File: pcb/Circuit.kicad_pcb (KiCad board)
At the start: 2 copper layers, 82.4 x 68.9 mm, 47 parts, among them J1 DTM13-12PA-R008, J2 TSW-101-07-T-D, J3 TSW-101-07-T-D, U1 MCP1700-1802E_TO92, U2 CDP68HC68S1, U3 LM2672N-5.0, U4 Teensy4.0, U5 MCP2562-H-P

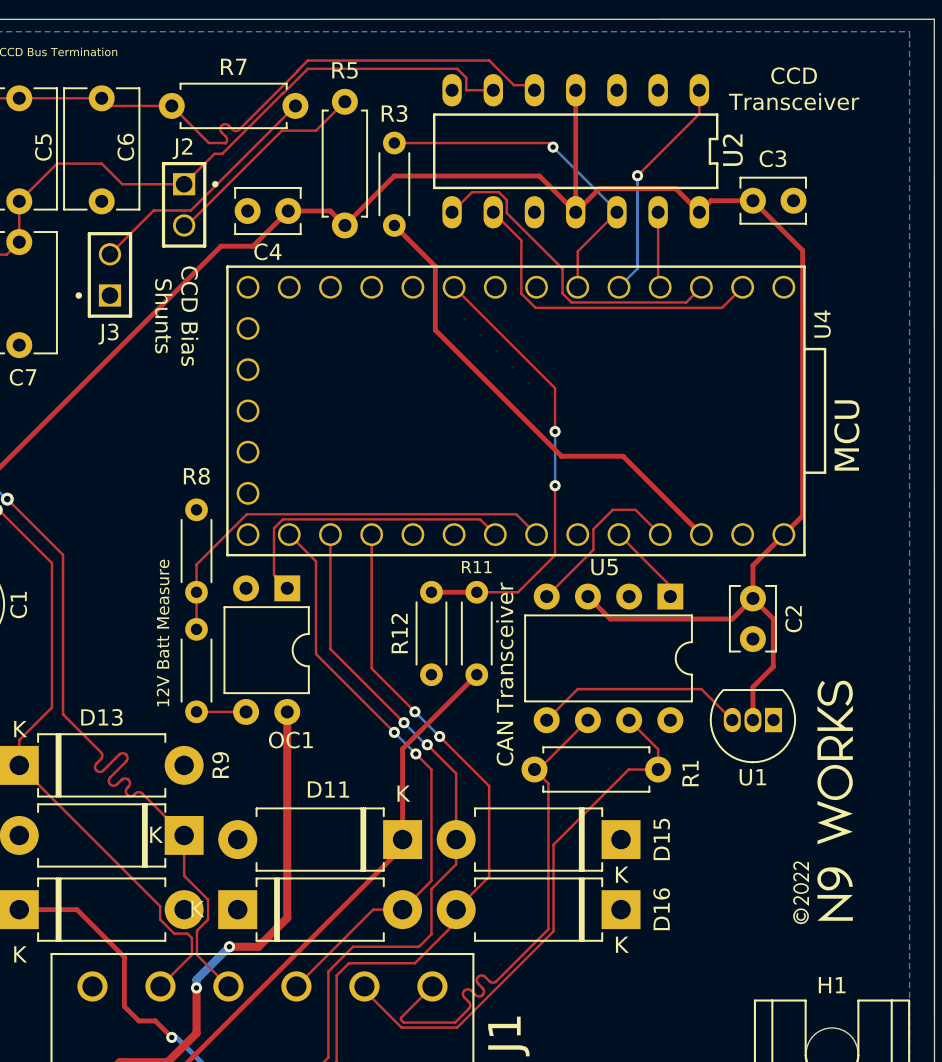
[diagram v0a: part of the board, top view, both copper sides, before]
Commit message: Add overvoltage protection to the 12v measure pin
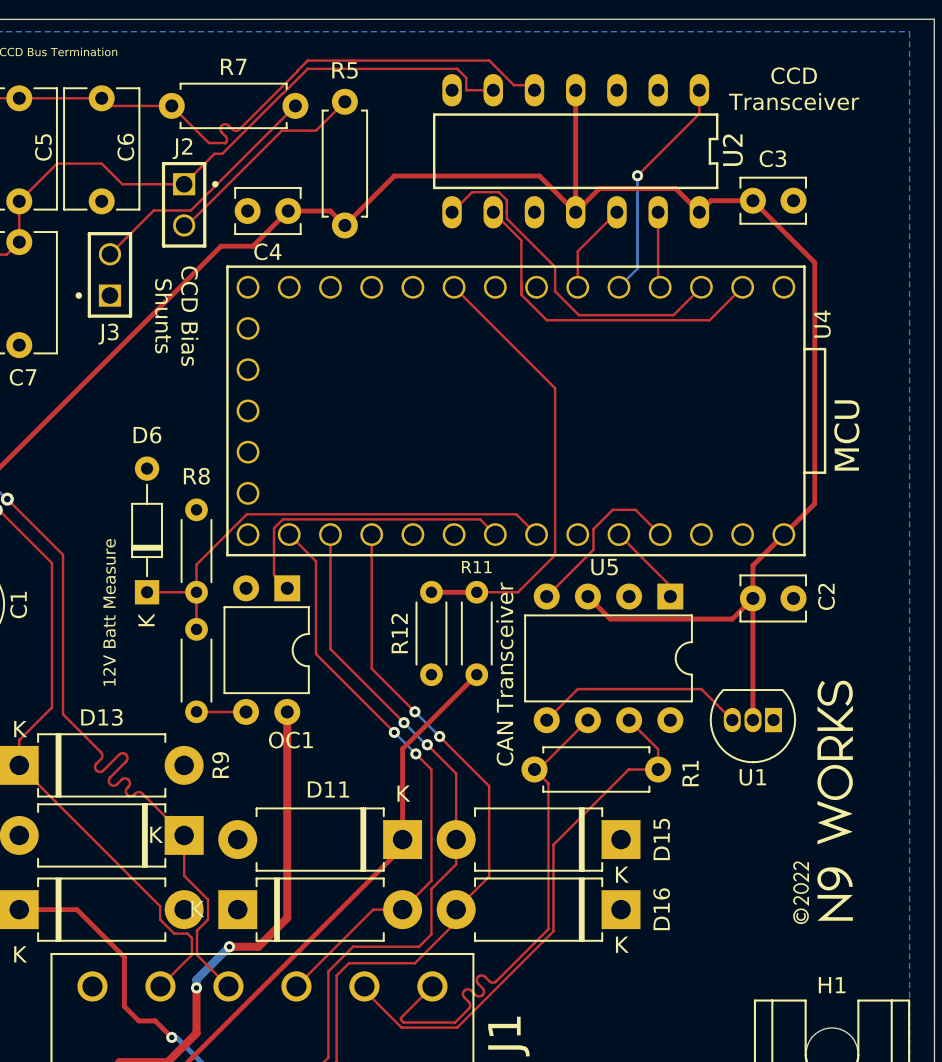
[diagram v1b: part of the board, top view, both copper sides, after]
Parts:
- removed R3: 10k, Resistor_THT:R_Axial_DIN0204_L3.6mm_D1.6mm_P5.08mm_Horizontal
- added D6: 3.3v Shottky, Diode_THT:D_DO-34_SOD68_P7.62mm_Horizontal, F.Cu at (84.1, 101.9)
- turned C2 to 0 degrees
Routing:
- net 3v3: track 29.1 -> 0.00 mm
- net idle: track 21.2 -> 5.62 mm, vias 1 -> 0
- net 12V_MEASURE: track 26.7 -> 29.8 mm
- net rxd: track 20.3 -> 21.6 mm
- net txd: track 20.4 -> 21.5 mm
- net SPEEDO: track 28.0 -> 27.7 mm, vias 2 -> 0

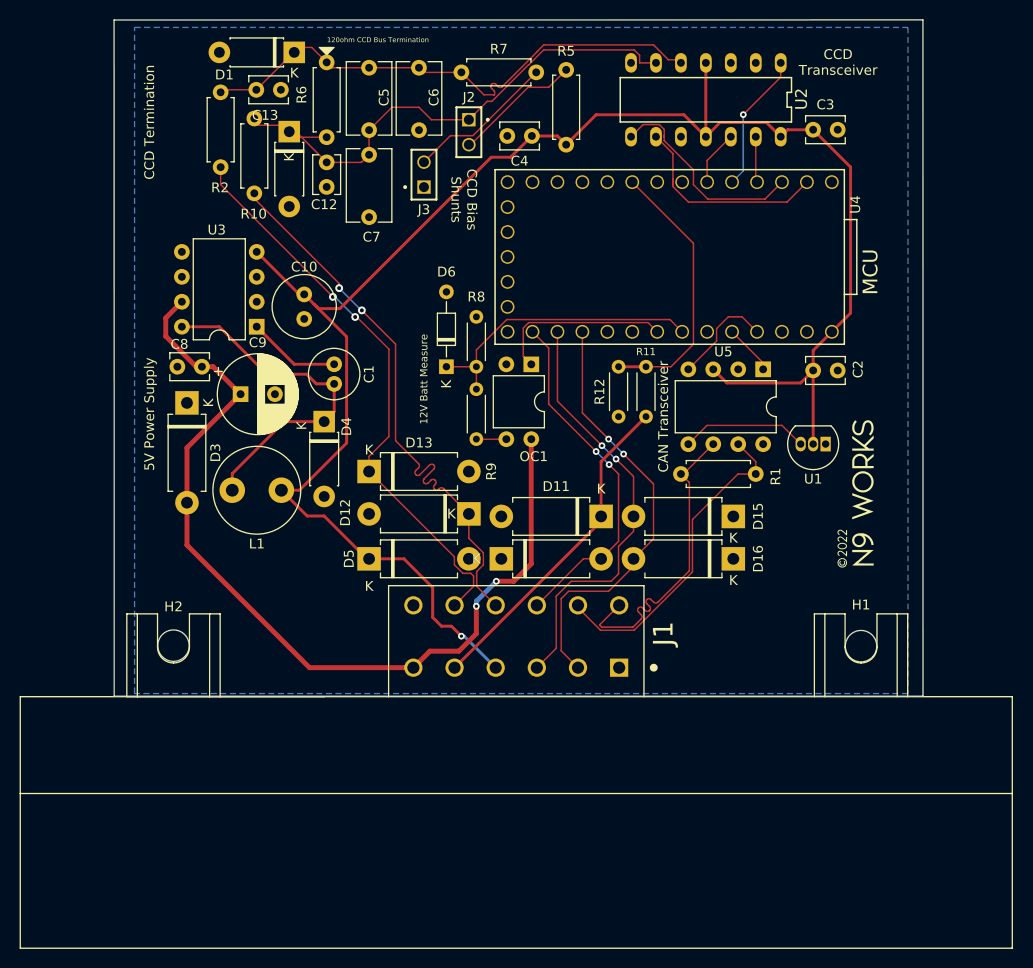
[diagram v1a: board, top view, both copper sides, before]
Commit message: Add 3.3v overvolt protection zeners
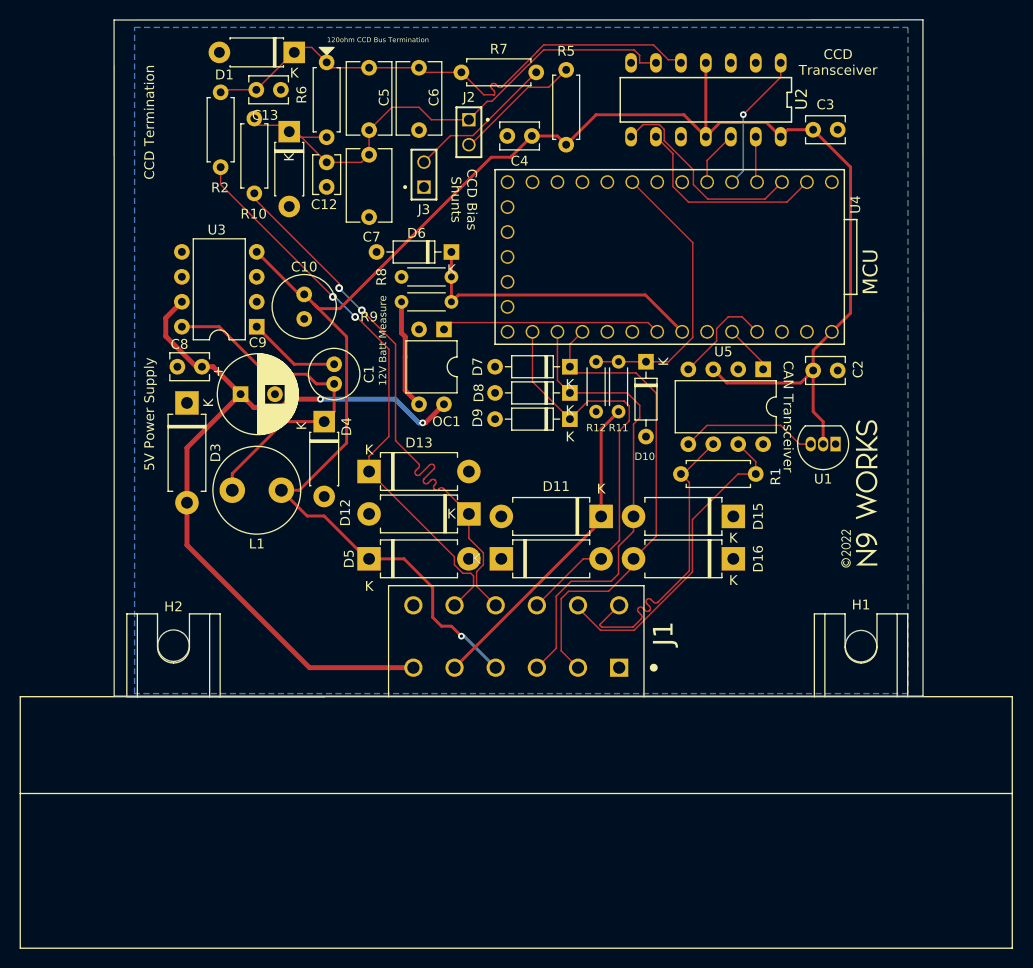
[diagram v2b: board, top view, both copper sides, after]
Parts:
- added D10: 3.3v, Diode_THT:D_DO-35_SOD27_P7.62mm_Horizontal, F.Cu at (104.4, 101.3)
- added D7: 3.3v, Diode_THT:D_DO-35_SOD27_P7.62mm_Horizontal, F.Cu at (96.6, 101.9)
- added D8: 3.3v, Diode_THT:D_DO-35_SOD27_P7.62mm_Horizontal, F.Cu at (96.6, 104.5)
- added D9: 3.3v, Diode_THT:D_DO-35_SOD27_P7.62mm_Horizontal, F.Cu at (96.6, 107.2)
- D6: value 3.3v Shottky -> 3.3v; footprint Diode_THT:D_DO-34_SOD68_P7.62mm_Horizontal -> Diode_THT:D_DO-35_SOD27_P7.62mm_Horizontal
- R8: value 1.5M -> 2.2Kohm
- R9: value 10M -> 13Kohm
- moved D6 11.7 mm to (84.6, 90.2), turned to 180 degrees
- moved OC1 9.57 mm to (83.8, 98.1)
- moved R8 9.49 mm to (84.6, 92.7), turned to 180 degrees
- moved R9 9.25 mm to (84.6, 95.2), turned to 180 degrees
- moved R11 2.84 mm to (101.6, 101.3)
- moved R12 2.34 mm to (99.3, 106.4)
- moved U1 1.02 mm to (123.7, 109.7)
- moved     0.38 mm to (126.1, 114.8)
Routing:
- net Net-(OC1-Pad3): track 3.06 -> 11.2 mm
- net +12V: track 91.1 -> 83.5 mm
- net IO/3: track 36.0 -> 42.7 mm, vias 2 -> 0
- net IO/1: track 44.2 -> 49.0 mm, vias 2 -> 0
- net 12V_MEASCTL: track 18.3 -> 22.4 mm
- net IO/2: track 43.9 -> 47.8 mm, vias 2 -> 0
- net SPEEDO: track 27.7 -> 29.2 mm
- net /1v8: track 13.0 -> 14.0 mm
- net rxd: track 21.6 -> 20.9 mm
- net SPEEDO_IN: track 33.6 -> 33.0 mm
- net 12V_MEASURE: track 29.8 -> 30.4 mm

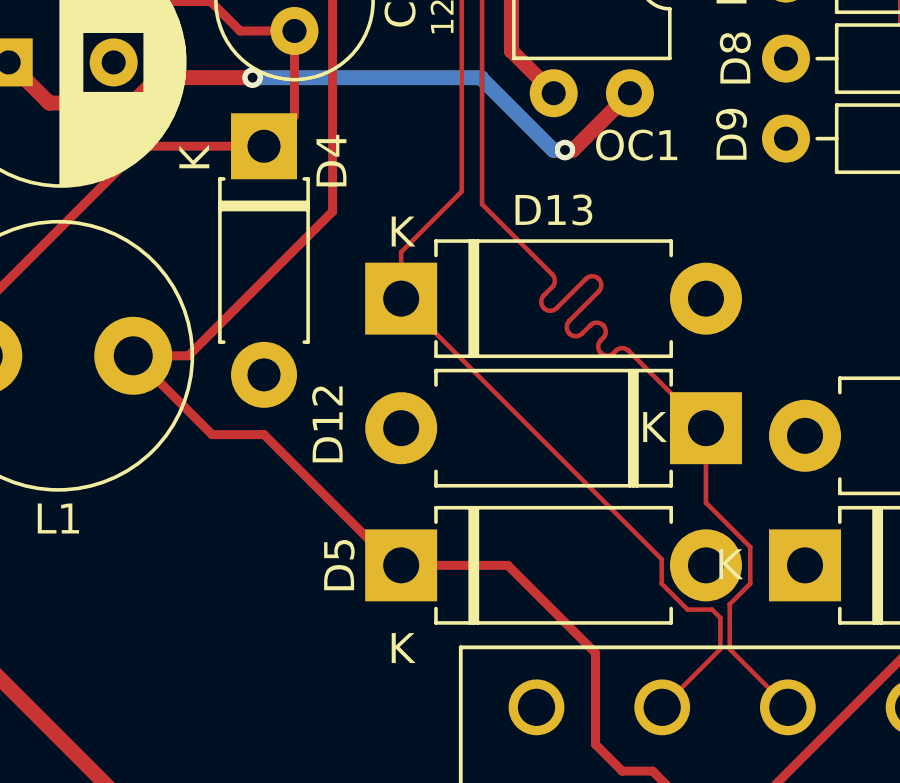
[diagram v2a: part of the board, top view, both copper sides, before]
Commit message: Use correctly sized TVS diodes for the CCD bus
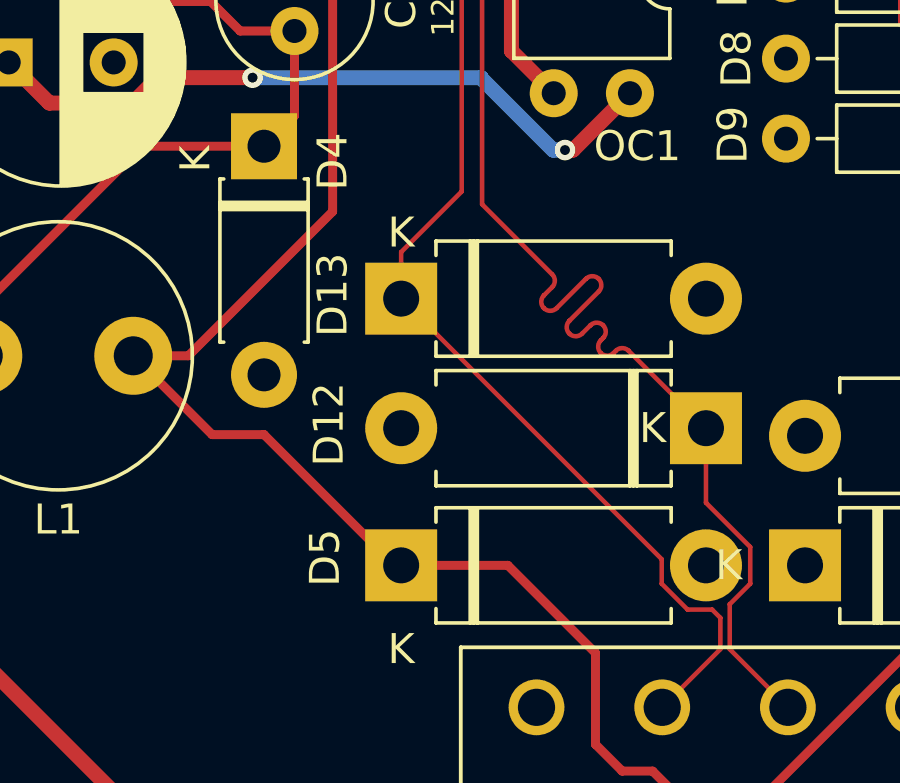
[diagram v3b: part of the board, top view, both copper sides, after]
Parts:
- D12, D13: value P6KE6.8A -> SA5.0CA
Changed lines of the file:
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@@
     (property "Sheetname" "")
     (attr through_hole)
-    (fp_text reference "D13" (at 5.08 -2.92) (layer "F.SilkS")
-      (effects (font (size 1 1) (thickness 0.15)))
-    )
-    (fp_text value "P6KE6.8A" (at 5.08 2.92) (layer "F.Fab")
+    (fp_text reference "D13" (at -2.286 -0.127 90) (layer "F.SilkS")
+      (effects (font (size 1 1) (thickness 0.15)))
+    )
+    (fp_text value "SA5.0CA" (at 5.08 2.92) (layer "F.Fab")
       (effects (font (size 1 1) (thickness 0.15)))
     )
@@
     (property "Sheetname" "")
     (attr through_hole)
-    (fp_text reference "D5" (at -2.032 0 90) (layer "F.SilkS")
+    (fp_text reference "D5" (at -2.54 -0.254 90) (layer "F.SilkS")
       (effects (font (size 1 1) (thickness 0.15)))
     )
@@
       (effects (font (size 1 1) (thickness 0.15)))
     )
-    (fp_text value "P6KE6.8A" (at 5.08 2.92 180) (layer "F.Fab")
-      (effects (font (size 1 1) (thickness 0.15)))
-    )
+    (fp_text value "SA5.0CA" (at 5.08 2.92 180) (layer "F.Fab")
+      (effects (font (size 1 1) (thickness 0.15)))
+    )

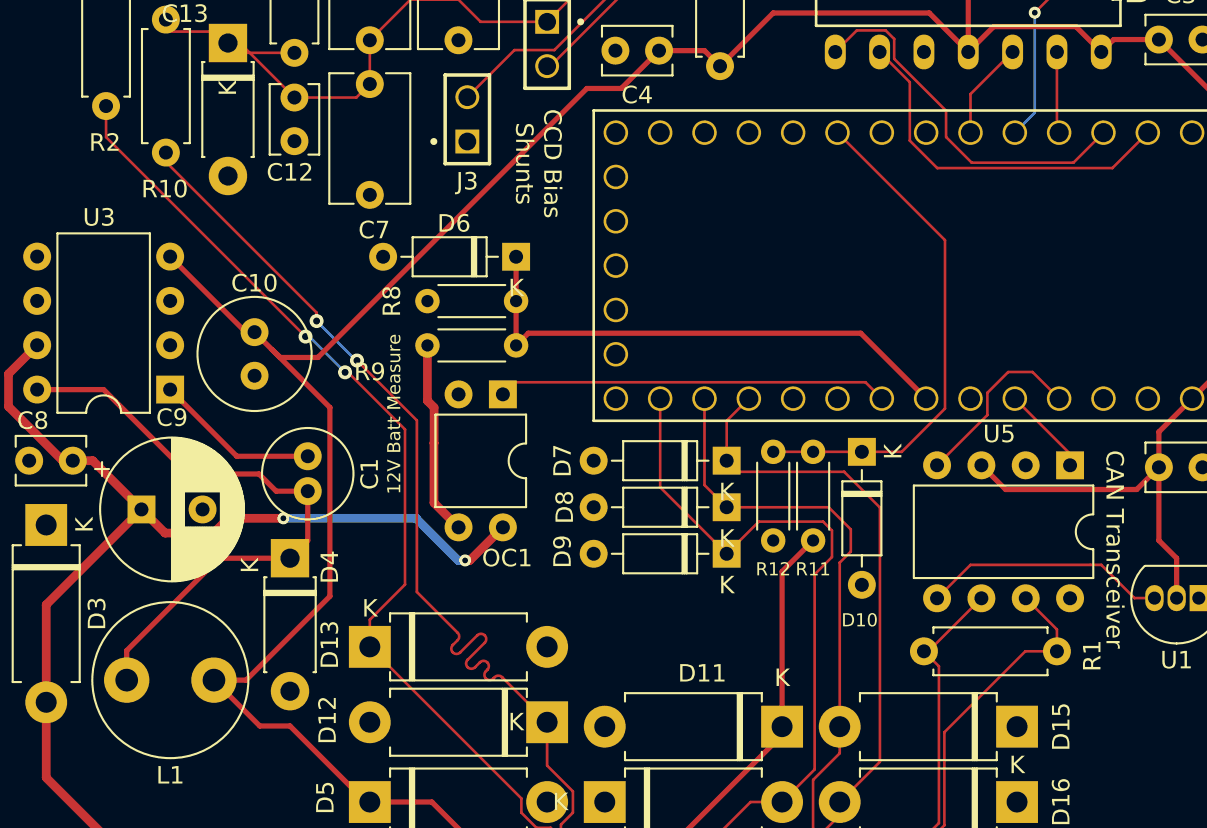
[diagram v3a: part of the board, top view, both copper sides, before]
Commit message: Move CCD lines farther from power
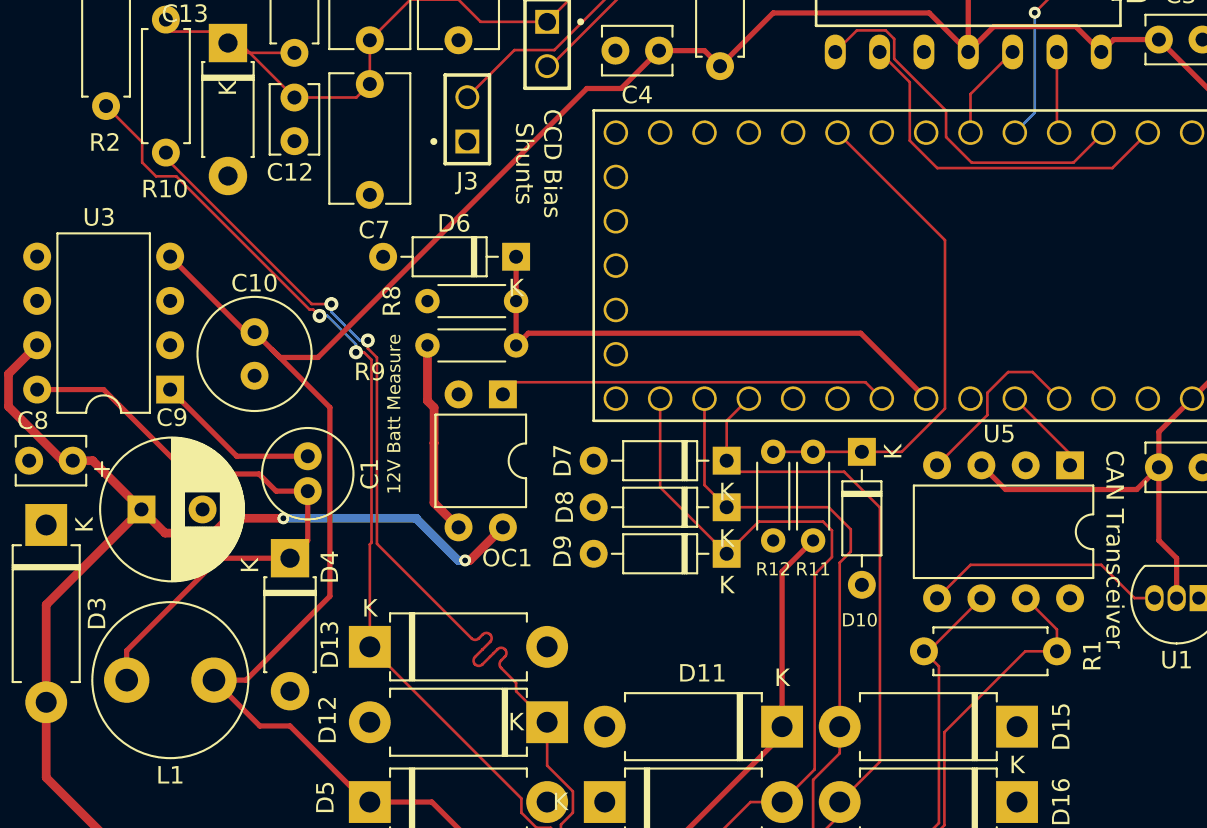
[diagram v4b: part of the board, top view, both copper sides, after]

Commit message: More tweaks
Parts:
- moved D10 0.99 mm to (103.8, 102.1)
- moved D7 0.99 mm to (96.0, 102.6)
- moved D8 0.99 mm to (96.0, 105.3)
- moved D9 0.99 mm to (96.0, 108.0)
- moved R11 0.99 mm to (101.0, 102.1)
- moved R12 0.99 mm to (98.7, 107.2)
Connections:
- J1 pad 4: +5V -> SPEEDO_IN
- J1 pad 5: SPEEDO_IN -> +5V
- U4 pad 31: 3v3 -> unconnected-(U4-Pad31)
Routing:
- net IO/3: track 42.7 -> 50.3 mm
- net IO/2: track 47.8 -> 54.9 mm
- net +5V: track 180.0 -> 176.5 mm, vias 1 -> 0
- net IO/1: track 49.0 -> 51.7 mm
- net SPEEDO_IN: track 33.0 -> 30.8 mm
- net SPEEDO: track 29.2 -> 29.9 mm
- net +12V: track 83.5 -> 83.8 mm, vias 2 -> 0
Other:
- board text added: "XJ/TJ CAN/CCD Instrument Cluster Adapter v1.0 © 2022 Scott Miller/N9 Works"
- board text removed: "XJ/TJ CAN/CCD Instrument Cluster Adapter © 2022 Scott Miller/N9 Works"
